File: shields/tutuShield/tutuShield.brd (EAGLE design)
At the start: 22.8 x 22.9 mm, 20 parts, among them IC1 IC_MSGEQ7-SOIC8

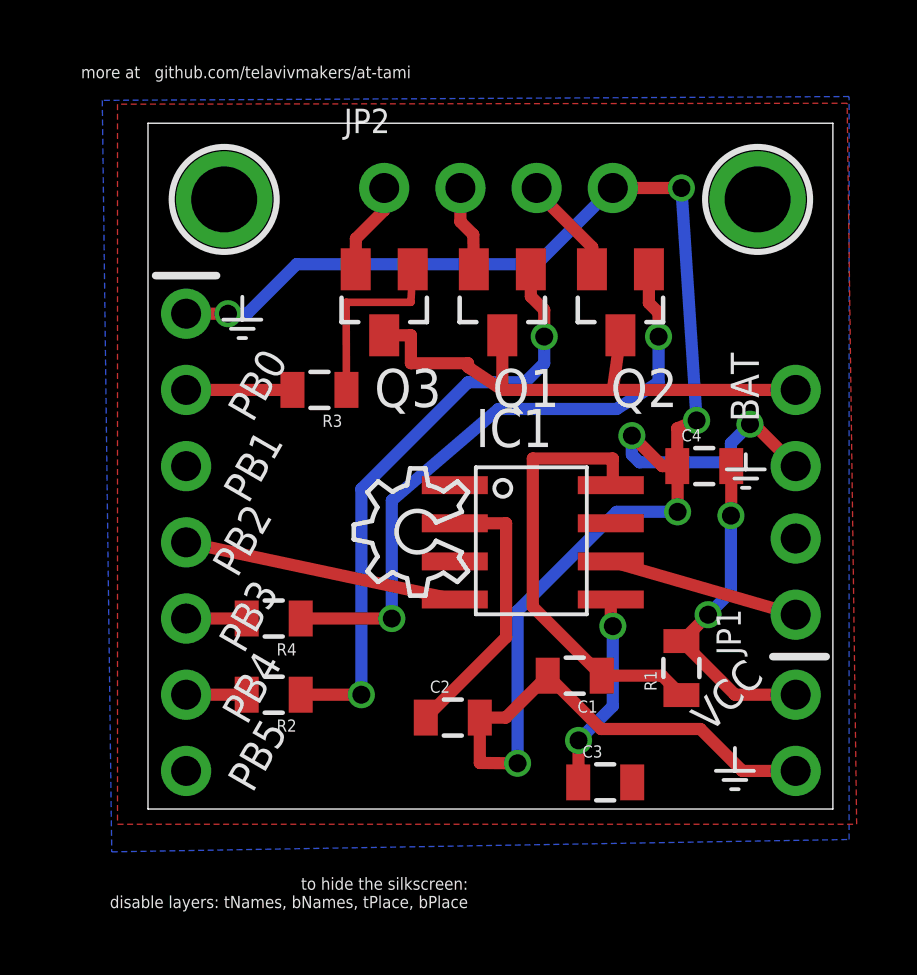
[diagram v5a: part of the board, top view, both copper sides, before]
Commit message: routed
without the PB5
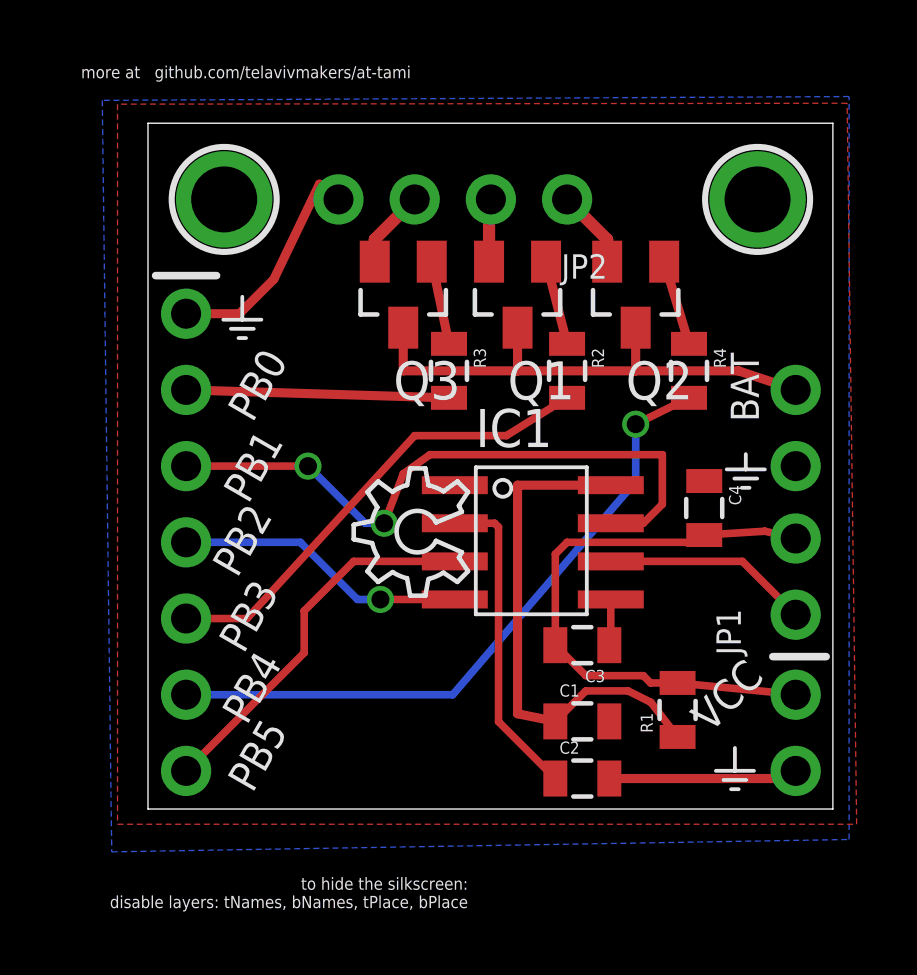
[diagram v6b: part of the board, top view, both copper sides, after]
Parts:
- moved R4 16.1 mm to (18.0, 14.6), turned to 270 degrees
- moved R2 14.6 mm to (14.0, 14.6), turned to 270 degrees
- moved C2 4.77 mm to (14.5, 1.02)
- moved C3 4.64 mm to (14.5, 5.46), turned to 180 degrees
- moved R3 4.36 mm to (10.0, 14.6), turned to 270 degrees
- moved JP2 1.57 mm to (10.2, 20.3), turned to 180 degrees
- moved C1 1.55 mm to (14.5, 2.92), turned to 0 degrees
- moved R1 1.40 mm to (17.7, 3.30)
- moved C4 1.40 mm to (18.5, 10.0), turned to 270 degrees
- moved Q3 0.68 mm to (8.51, 17.1)
- moved Q1 0.57 mm to (12.3, 17.1)
- moved Q2 0.57 mm to (16.3, 17.1)
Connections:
- net N$10: now also JP2.1; no longer JP2.3
- net N$13: now also JP2.3; no longer JP2.1
- net PB3: now also R2.2; no longer R4.2
- net PB4: now also R4.2; no longer R2.2
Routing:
- net GND: track 66.4 -> 14.0 mm, vias 7 -> 0
- net PB1: track 0.00 -> 21.6 mm, vias 0 -> 2
- net PB4: track 2.02 -> 22.1 mm, vias 0 -> 1
- net N$7: track 21.2 -> 2.86 mm, vias 2 -> 0
- net N$6: track 20.0 -> 2.83 mm, vias 2 -> 0
- net PB3: track 2.02 -> 15.7 mm
- net PB5: track 0.00 -> 12.7 mm
- net VCC: track 11.1 -> 19.9 mm, vias 2 -> 0
- net PB0: track 3.55 -> 8.77 mm
- net IN: track 6.60 -> 1.54 mm, vias 2 -> 0
- net N$3: track 6.18 -> 2.80 mm
- net CKIN: track 14.7 -> 17.2 mm
- net N$5: track 9.30 -> 10.8 mm
- net V_BAT: track 18.7 -> 17.5 mm
- net N$10: track 3.48 -> 2.63 mm
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
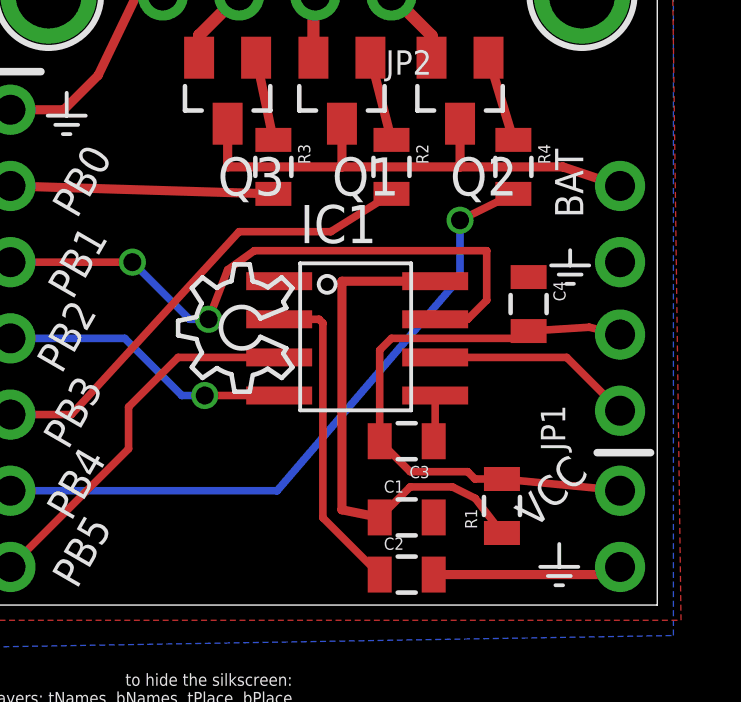
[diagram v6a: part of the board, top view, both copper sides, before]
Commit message: fix GND and VCC airwires
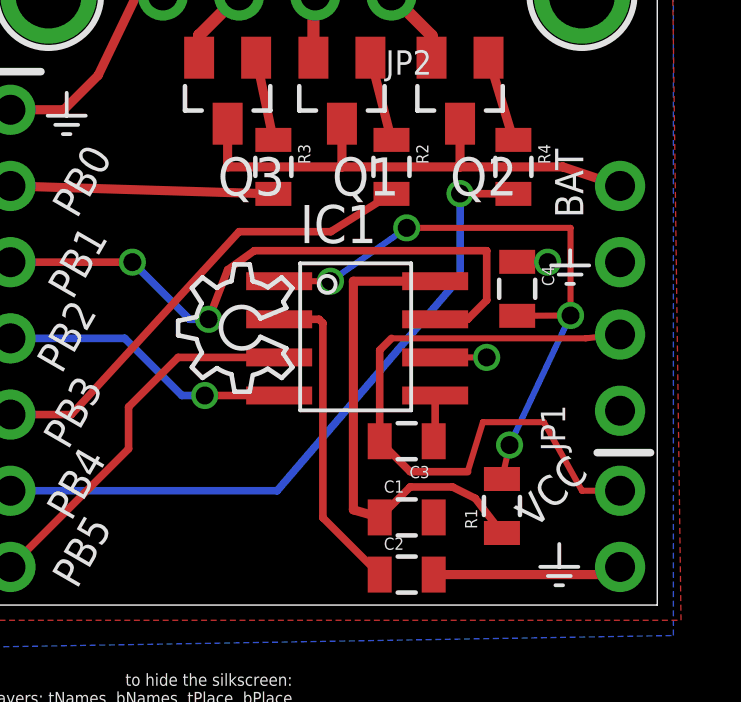
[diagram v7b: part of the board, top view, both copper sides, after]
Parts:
- moved C4 0.64 mm to (18.2, 10.5)
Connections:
- removed net N$4: IC1.6, JP1.1
- new net VDDA: C4.2, IC1.1, R1.2
- net GND: now also IC1.6, JP1.1
- net VCC: no longer C4.2, R1.2
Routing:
- net VDDA: track 0.00 -> 20.9 mm, vias 0 -> 4
- net N$4: track 6.90 -> 0.00 mm
- net GND: track 14.0 -> 17.2 mm, vias 0 -> 2
- net VCC: track 19.9 -> 22.2 mm
- net CKIN: track 17.2 -> 16.4 mm
- net PB4: track 22.1 -> 22.8 mm
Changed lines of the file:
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@@
 <?xml version="1.0" encoding="utf-8"?>
 <!DOCTYPE eagle SYSTEM "eagle.dtd">
-<eagle version="7.1.0">
+<eagle version="7.2.0">
 <drawing>
 <settings>
@@
 <element name="C2" library="ATtami" package="0805" value="0.1uF" x="14.478" y="1.016"/>
 <element name="C3" library="ATtami" package="0805" value="1000pF" x="14.478" y="5.461" rot="R180"/>
-<element name="C4" library="ATtami" package="0805" value="0.1uF" x="18.542" y="10.033" rot="R270"/>
+<element name="C4" library="ATtami" package="0805" value="0.1uF" x="18.161" y="10.541" rot="R270"/>
 <element name="JP1" library="ATtami" package="1X02_ROUND" value="" x="21.59" y="7.747" rot="R90"/>
 <element name="R1" library="ATtami" package="0805" value="200K" x="17.653" y="3.302" rot="R90"/>
@@
 <wire x1="15.378" y1="1.016" x2="21.336" y2="1.016" width="0.3048" layer="1"/>
 <wire x1="21.336" y1="1.016" x2="21.59" y2="1.27" width="0.3048" layer="1"/>
+<contactref element="JP1" pad="1"/>
+<contactref element="IC1" pad="6"/>
+<wire x1="21.59" y1="6.477" x2="21.59" y2="11.43" width="0" layer="19" extent="1-1"/>
+<wire x1="21.59" y1="1.27" x2="21.59" y2="6.477" width="0" layer="19" extent="1-1"/>
+<wire x1="15.378" y1="2.921" x2="15.378" y2="1.016" width="0" layer="19" extent="1-1"/>
+<wire x1="4.191" y1="17.653" x2="15.427" y2="8.255" width="0" layer="19" extent="1-1"/>
+<wire x1="18.161" y1="11.441" x2="19.177" y2="11.43" width="0.2032" layer="1"/>
+<wire x1="15.427" y1="8.255" x2="17.145" y2="8.255" width="0.2032" layer="1"/>
+<via x="17.145" y="8.255" extent="1-16" drill="0.6" shape="square"/>
+<wire x1="17.145" y1="8.255" x2="17.399" y2="8.255" width="0.2032" layer="16"/>
+<wire x1="17.399" y1="8.255" x2="18.161" y2="11.441" width="0" layer="19" extent="1-16"/>
+<via x="19.177" y="11.43" extent="1-16" drill="0.6" shape="square"/>
+<wire x1="19.177" y1="11.43" x2="19.304" y2="11.43" width="0.2032" layer="16"/>
+<wire x1="19.304" y1="11.43" x2="21.59" y2="11.43" width="0" layer="19" extent="1-16"/>
 </signal>
 <signal name="VCC">
 <contactref element="J3" pad="1"/>
-<contactref element="C4" pad="2"/>
-<contactref element="R1" pad="2"/>
 <contactref element="C3" pad="2"/>
 <contactref element="JP1" pad="2"/>
-<wire x1="17.653" y1="4.202" x2="21.579" y2="3.821" width="0.254" layer="1"/>
 <wire x1="21.579" y1="3.821" x2="21.59" y2="3.81" width="0.254" layer="1"/>
-<wire x1="18.542" y1="9.133" x2="20.563" y2="9.26" width="0.254" layer="1"/>
-<wire x1="20.563" y1="9.26" x2="21.59" y2="9.017" width="0.254" layer="1"/>
-<wire x1="17.653" y1="4.202" x2="16.753" y2="4.202" width="0.254" layer="1"/>
-<wire x1="16.753" y1="4.202" x2="16.51" y2="4.445" width="0.254" layer="1"/>
 <wire x1="16.51" y1="4.445" x2="14.594" y2="4.445" width="0.254" layer="1"/>
 <wire x1="14.594" y1="4.445" x2="13.578" y2="5.461" width="0.254" layer="1"/>
 <wire x1="13.578" y1="5.461" x2="13.578" y2="8.498" width="0.254" layer="1"/>
 <wire x1="13.578" y1="8.498" x2="13.97" y2="8.89" width="0.254" layer="1"/>
-<wire x1="13.97" y1="8.89" x2="18.045" y2="8.89" width="0.254" layer="1"/>
-<wire x1="18.045" y1="8.89" x2="18.542" y2="9.133" width="0.254" layer="1"/>
+<wire x1="21.59" y1="3.81" x2="20.32" y2="3.81" width="0.2032" layer="1"/>
+<wire x1="20.32" y1="3.81" x2="19.05" y2="6.096" width="0.2032" layer="1"/>
+<wire x1="19.05" y1="6.096" x2="17.018" y2="6.096" width="0.2032" layer="1"/>
+<wire x1="17.018" y1="6.096" x2="16.51" y2="4.445" width="0.2032" layer="1"/>
+<wire x1="21.59" y1="9.017" x2="20.447" y2="8.89" width="0.2032" layer="1"/>
+<wire x1="20.447" y1="8.89" x2="13.97" y2="8.89" width="0.2032" layer="1"/>
 </signal>
 <signal name="N$2">
@@
 <wire x1="1.27" y1="3.81" x2="10.16" y2="3.81" width="0.254" layer="16"/>
 <wire x1="10.16" y1="3.81" x2="16.256" y2="10.922" width="0.254" layer="16"/>
-<wire x1="16.256" y1="10.922" x2="16.256" y2="12.827" width="0.254" layer="16"/>
-<via x="16.256" y="12.827" extent="1-16" drill="0.6" shape="square"/>
-<wire x1="16.256" y1="12.827" x2="18.034" y2="13.705" width="0.254" layer="1"/>
+<wire x1="16.256" y1="10.922" x2="16.256" y2="13.716" width="0.254" layer="16"/>
+<via x="16.256" y="13.716" extent="1-16" drill="0.6" shape="square"/>
+<wire x1="16.256" y1="13.716" x2="18.034" y2="13.705" width="0.254" layer="1"/>
 </signal>
 <signal name="PB5">
@@
 <wire x1="15.427" y1="6.985" x2="15.427" y2="5.51" width="0.254" layer="1"/>
 <wire x1="15.427" y1="5.51" x2="15.378" y2="5.461" width="0.254" layer="1"/>
-</signal>
-<signal name="N$4">
-<contactref element="IC1" pad="6"/>
-<contactref element="JP1" pad="1"/>
-<wire x1="15.427" y1="8.255" x2="19.812" y2="8.255" width="0.254" layer="1"/>
-<wire x1="19.812" y1="8.255" x2="21.59" y2="6.477" width="0.254" layer="1"/>
 </signal>
 <signal name="N$5">
@@
 <contactref element="C1" pad="1"/>
 <contactref element="R1" pad="1"/>
-<wire x1="15.427" y1="10.795" x2="12.319" y2="10.795" width="0.3048" layer="1"/>
-<wire x1="12.319" y1="10.795" x2="12.319" y2="3.175" width="0.3048" layer="1"/>
-<wire x1="12.319" y1="3.175" x2="13.578" y2="2.921" width="0.3048" layer="1"/>
+<wire x1="15.427" y1="10.795" x2="12.7" y2="10.795" width="0.3048" layer="1"/>
+<wire x1="12.7" y1="10.795" x2="12.7" y2="3.175" width="0.3048" layer="1"/>
+<wire x1="12.7" y1="3.175" x2="13.578" y2="2.921" width="0.3048" layer="1"/>
 <wire x1="17.653" y1="2.402" x2="16.764" y2="3.556" width="0.254" layer="1"/>
 <wire x1="16.764" y1="3.556" x2="16.002" y2="3.937" width="0.254" layer="1"/>
@@
 <wire x1="7.559" y1="18.989" x2="8.89" y2="20.32" width="0.4064" layer="1"/>
 </signal>
+<signal name="VDDA">
+<contactref element="C4" pad="2"/>
+<contactref element="R1" pad="2"/>
+<contactref element="IC1" pad="1"/>
+<wire x1="17.653" y1="4.202" x2="17.907" y2="5.334" width="0.2032" layer="1"/>
+<via x="17.907" y="5.334" extent="1-16" drill="0.6" shape="square"/>
+<wire x1="17.907" y1="5.334" x2="19.939" y2="9.652" width="0.2032" layer="16"/>
+<via x="19.939" y="9.652" extent="1-16" drill="0.6" shape="square"/>
+<wire x1="19.939" y1="9.652" x2="18.161" y2="9.641" width="0.2032" layer="1"/>
+<wire x1="10.227" y1="10.795" x2="11.938" y2="10.795" width="0.2032" layer="1"/>
+<via x="11.938" y="10.795" extent="1-16" drill="0.6" shape="square"/>
+<wire x1="11.938" y1="10.795" x2="14.478" y2="12.573" width="0.2032" layer="16"/>
+<via x="14.478" y="12.573" extent="1-16" drill="0.6" shape="square"/>
+<wire x1="14.478" y1="12.573" x2="19.939" y2="12.573" width="0.2032" layer="1"/>
+<wire x1="19.939" y1="12.573" x2="19.939" y2="9.652" width="0.2032" layer="1"/>
+</signal>
 </signals>

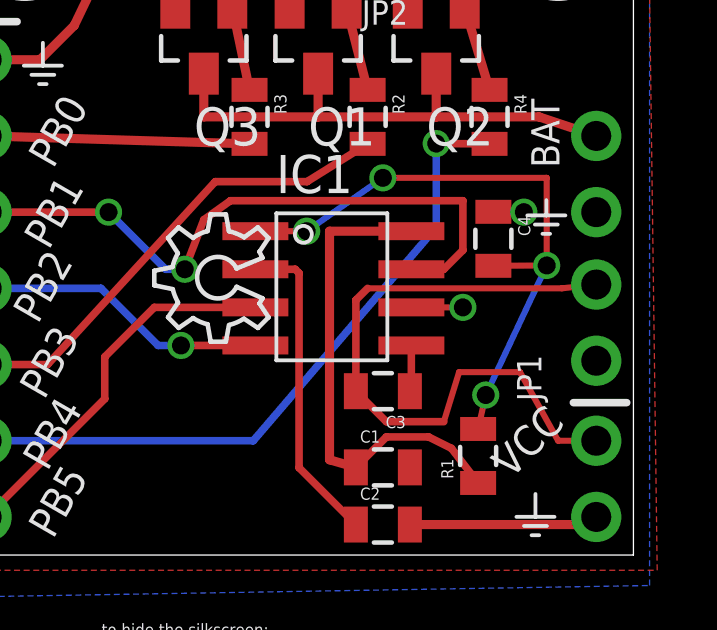
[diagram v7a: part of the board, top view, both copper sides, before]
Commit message: Moved via because of DRC rules
Moved via next to the main chip because of DRC rules and 'ratsnest'ed it
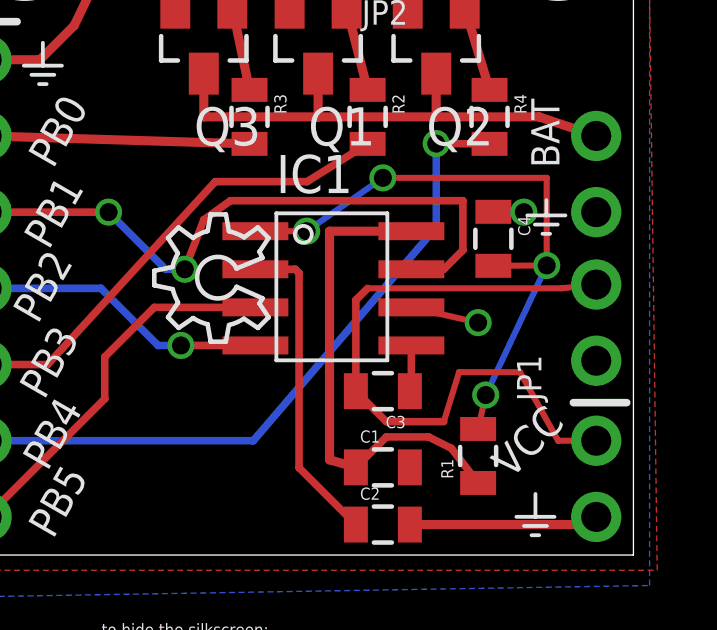
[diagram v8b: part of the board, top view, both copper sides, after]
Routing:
- net GND: track 17.2 -> 17.7 mm
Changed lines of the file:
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@@
 </class>
 </classes>
-<designrules name="dirt_cheap_dirty_boards.v1">
-<description language="en">&lt;b&gt;Dirty Cheap Dirty Board Design Rules&lt;/b&gt;
-&lt;br&gt;
-&lt;br&gt;Min width/Spacing: 5/5mil
-&lt;br&gt;Min diameter of finished hole 12mil</description>
+<designrules name="Elecrow_2-layer_eagle_rule">
+<description language="de">&lt;b&gt;EAGLE Design Rules&lt;/b&gt;
+&lt;p&gt;
+Die Standard-Design-Rules sind so gewählt, dass sie für
+die meisten Anwendungen passen. Sollte ihre Platine
+besondere Anforderungen haben, treffen Sie die erforderlichen
+Einstellungen hier und speichern die Design Rules unter
+einem neuen Namen ab.</description>
+<description language="en">&lt;b&gt;EAGLE Design Rules&lt;/b&gt;
+&lt;p&gt;
+The default Design Rules have been set to cover
+a wide range of applications. Your particular design
+may have different requirements, so please make the
+necessary adjustments and save your customized
+design rules under a new name.</description>
+<description language="zh">&lt;b&gt;Elecrow EAGLE Design Rules&lt;/b&gt;
+</description>
 <param name="layerSetup" value="(1*16)"/>
-<param name="mtCopper" value="0.035mm 0.0175mm 0.035mm 0.035mm 0.035mm 0.035mm 0.035mm 0.035mm 0.035mm 0.035mm 0.035mm 0.035mm 0.035mm 0.035mm 0.0175mm 0.035mm"/>
-<param name="mtIsolate" value="1.5mm 1.1mm 0.2mm 0.15mm 0.2mm 0.15mm 0.2mm 0.15mm 0.2mm 0.15mm 0.2mm 0.15mm 0.2mm 0.15mm 0.2mm"/>
-<param name="mdWireWire" value="5mil"/>
-<param name="mdWirePad" value="5mil"/>
-<param name="mdWireVia" value="5mil"/>
-<param name="mdPadPad" value="5mil"/>
-<param name="mdPadVia" value="5mil"/>
-<param name="mdViaVia" value="5mil"/>
+<param name="mtCopper" value="0.035mm 0.035mm 0.035mm 0.035mm 0.035mm 0.035mm 0.035mm 0.035mm 0.035mm 0.035mm 0.035mm 0.035mm 0.035mm 0.035mm 0.035mm 0.035mm"/>
+<param name="mtIsolate" value="1.5mm 0.15mm 0.2mm 0.15mm 0.2mm 0.15mm 0.2mm 0.15mm 0.2mm 0.15mm 0.2mm 0.15mm 0.2mm 0.15mm 0.2mm"/>
+<param name="mdWireWire" value="6mil"/>
+<param name="mdWirePad" value="6mil"/>
+<param name="mdWireVia" value="6mil"/>
+<param name="mdPadPad" value="6mil"/>
+<param name="mdPadVia" value="6mil"/>
+<param name="mdViaVia" value="6mil"/>
 <param name="mdSmdPad" value="0mil"/>
 <param name="mdSmdVia" value="0mil"/>
@@
 <param name="mdDrill" value="10mil"/>
 <param name="mdSmdStop" value="0mil"/>
-<param name="msWidth" value="5mil"/>
+<param name="msWidth" value="6mil"/>
 <param name="msDrill" value="12mil"/>
 <param name="msMicroVia" value="12mil"/>
@@
 <param name="mlMinCreamFrame" value="0mil"/>
 <param name="mlMaxCreamFrame" value="0mil"/>
-<param name="mlViaStopLimit" value="25mil"/>
+<param name="mlViaStopLimit" value="100mil"/>
 <param name="srRoundness" value="0"/>
 <param name="srMinRoundness" value="0mil"/>
@@
 <contactref element="JP1" pad="1"/>
 <contactref element="IC1" pad="6"/>
-<wire x1="21.59" y1="6.477" x2="21.59" y2="11.43" width="0" layer="19" extent="1-1"/>
-<wire x1="21.59" y1="1.27" x2="21.59" y2="6.477" width="0" layer="19" extent="1-1"/>
-<wire x1="15.378" y1="2.921" x2="15.378" y2="1.016" width="0" layer="19" extent="1-1"/>
-<wire x1="4.191" y1="17.653" x2="15.427" y2="8.255" width="0" layer="19" extent="1-1"/>
 <wire x1="18.161" y1="11.441" x2="19.177" y2="11.43" width="0.2032" layer="1"/>
-<wire x1="15.427" y1="8.255" x2="17.145" y2="8.255" width="0.2032" layer="1"/>
-<via x="17.145" y="8.255" extent="1-16" drill="0.6" shape="square"/>
-<wire x1="17.145" y1="8.255" x2="17.399" y2="8.255" width="0.2032" layer="16"/>
-<wire x1="17.399" y1="8.255" x2="18.161" y2="11.441" width="0" layer="19" extent="1-16"/>
+<wire x1="15.427" y1="8.255" x2="17.653" y2="7.747" width="0.2032" layer="1"/>
+<via x="17.653" y="7.747" extent="1-16" drill="0.6" shape="square"/>
+<wire x1="17.653" y1="7.747" x2="17.907" y2="7.747" width="0.2032" layer="16"/>
 <via x="19.177" y="11.43" extent="1-16" drill="0.6" shape="square"/>
 <wire x1="19.177" y1="11.43" x2="19.304" y2="11.43" width="0.2032" layer="16"/>
-<wire x1="19.304" y1="11.43" x2="21.59" y2="11.43" width="0" layer="19" extent="1-16"/>
 </signal>
 <signal name="VCC">
